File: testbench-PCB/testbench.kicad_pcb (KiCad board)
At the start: 2 copper layers, 41 parts, among them J1 USB_C_Receptacle_USB2.0, J2 AVR-ISP, J3 AVR-JTAG, SW1 SW_Push, U1 ATmega2561-16A, U10 CH340C, U2 Thermistor_module, U3 Rotary_encoder_switch_module, U4 RTC_EEPROM_module, U5 ATmega328P_Xplained_Mini, U7 Matrix_keyboard, U9 USBLC6-2SC6, Y1 X322516MLB4SI

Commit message: Updated footprints, PCB.
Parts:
- added F1: Polyfuse, Fuse:Fuse_1812_4532Metric, F.Cu at (-84.2, 3.73)
- added U6: Relay_module, kit_modules:Relay_module, F.Cu at (164.1, 147.2)
- added U8: LCD_display, kit_modules:LCD_1602A_module, F.Cu at (67.1, 100.3)
- LS1, SW1, U7: moved to B.Cu
- U2: footprint Connector_PinSocket_2.54mm:PinSocket_1x04_P2.54mm_Horizontal -> Connector_PinSocket_2.54mm:PinSocket_1x04_P2.54mm_Vertical; moved to B.Cu
- U3: footprint Connector_PinSocket_2.54mm:PinSocket_1x05_P2.54mm_Horizontal -> kit_modules:Encoder_module
- U4: footprint Connector_PinSocket_2.54mm:PinSocket_1x06_P2.54mm_Horizontal -> Connector_PinSocket_2.54mm:PinSocket_1x06_P2.54mm_Vertical; moved to B.Cu
- moved U5 288.5 mm to (221.0, 101.6)
- moved U4 189.0 mm to (141.0, 115.6), turned to 180 degrees
- moved U2 153.1 mm to (121.9, 115.6), turned to 180 degrees
- moved J1 145.2 mm to (-96.5, -3.89), turned to -90 degrees
- moved U3 141.1 mm to (96.5, 109.2), turned to -90 degrees
- moved R7 133.4 mm to (-60.0, -29.3)
- moved J3 132.9 mm to (-25.3, -25.5), turned to 90 degrees
- moved R6 127.9 mm to (-45.6, -25.5)
- moved R5 123.7 mm to (-60.0, -25.5)
- moved TP2 117.5 mm to (-82.5, -12.8)
- moved FB1 116.1 mm to (-91.4, 5.00)
- moved U7 114.9 mm to (69.8, 111.8), turned to 180 degrees
- moved LS1 114.3 mm to (69.8, 141.0), turned to 180 degrees
- moved C6 113.1 mm to (-31.4, -2.62)
- moved C4 111.9 mm to (-25.3, -5.16), turned to 180 degrees
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
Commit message: Routed osc., USB interface.
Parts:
- added C1: 10u, Capacitor_SMD:C_0805_2012Metric, F.Cu at (36.4, 90.8)
- C2, C3: value 22n -> 22p
- moved TP1 155.5 mm to (35.1, 95.9)
- moved TP2 155.5 mm to (28.8, 95.9)
- moved J1 145.0 mm to (20.0, 82.5)
- moved U10 145.0 mm to (42.8, 83.8)
- moved U9 145.0 mm to (31.4, 82.5)
- moved FB1 144.1 mm to (24.3, 90.9)
- moved F1 143.7 mm to (30.7, 90.2)
- moved JP1 131.8 mm to (42.1, 75.0), turned to 90 degrees
- moved JP2 131.7 mm to (44.7, 75.0), turned to 90 degrees
- moved C5 128.3 mm to (74.6, 94.6)
- moved R8 127.0 mm to (79.0, 93.3), turned to 180 degrees
- moved C2 126.7 mm to (80.3, 96.5), turned to 90 degrees
- moved R4 125.7 mm to (74.6, 92.1), turned to 180 degrees
- moved C6 122.7 mm to (70.8, 65.4)
- moved C3 122.5 mm to (77.8, 96.5), turned to 90 degrees
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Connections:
- net Net-(F1-Pad1) renamed /USB Interface/VBUS
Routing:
- net +5V: track 0.00 -> 23.6 mm
- net Net-(J1-SHIELD): track 0.00 -> 21.1 mm
- net Net-(U10-UD+): track 0.00 -> 17.8 mm
- net Net-(U10-UD-): track 0.00 -> 17.6 mm
- net /USB Interface/VBUS: track 0.00 -> 16.2 mm, vias 0 -> 2
- net Net-(U1-XTAL1): track 0.00 -> 12.0 mm
- net /MCU/RST: track 0.00 -> 10.6 mm
- net Net-(U1-XTAL2): track 0.00 -> 10.5 mm
- net GND: track 0.00 -> 9.67 mm
- net Net-(JP2-A): track 0.00 -> 8.75 mm
- net Net-(J1-CC1): track 0.00 -> 7.16 mm
- net Net-(J1-CC2): track 0.00 -> 6.44 mm
- net Net-(JP1-A): track 0.00 -> 6.29 mm
- net Net-(U1-AREF): track 0.00 -> 4.92 mm
- net Net-(U10-V3): track 0.00 -> 3.88 mm

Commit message: Rearanged PCB, updated footprints.
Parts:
- added D1: LED, LED_SMD:LED_0805_2012Metric, F.Cu at (175.4, 154.4)
- added D2: LED, LED_SMD:LED_0805_2012Metric, F.Cu at (168.6, 154.2)
- added R15: 500R, Resistor_SMD:R_0805_2012Metric, F.Cu at (172.2, 148.0)
- added R16: 500R, Resistor_SMD:R_0805_2012Metric, F.Cu at (167.8, 148.0)
- LS1, SW1, U2, U4, U7: moved to F.Cu
- U5: value ATmega328P_Xplained_Mini -> ATmega328P_Xplained_mini; footprint kit_modules:ATmega328P_Xplained_Mini -> kit_modules:ATmega328P_Xplained_mini
- moved R11 172.5 mm to (211.4, 72.5)
- moved R10 172.5 mm to (211.4, 69.6)
- moved R12 172.5 mm to (211.4, 75.5)
- moved R9 172.5 mm to (211.4, 66.6)
- moved SW1 162.2 mm to (159.7, 152.4), turned to 0 degrees
- moved R3 153.7 mm to (157.8, 146.7), turned to 0 degrees
- moved J2 147.5 mm to (143.0, 153.1), turned to 90 degrees
- moved R5 145.4 mm to (138.1, 151.1)
- moved R6 145.4 mm to (152.4, 151.1)
- moved R7 145.4 mm to (138.1, 147.3)
- moved R13 143.6 mm to (133.0, 42.2), turned to -90 degrees
- moved R14 127.6 mm to (60.3, 43.7)
- moved U6 124.5 mm to (142.5, 38.7), turned to 180 degrees
- moved J3 115.9 mm to (118.5, 151.8)
- moved LS1 115.8 mm to (59.9, 36.1), turned to 0 degrees
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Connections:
- U1 pad 30: unconnected-(U1-PD5-Pad30) -> /ATmega328P module/DUT_D4
- U1 pad 31: unconnected-(U1-PD6-Pad31) -> /ATmega328P module/DUT_D3
- U1 pad 32: unconnected-(U1-PD7-Pad32) -> /ATmega328P module/DUT_D2
- U1 pad 33: unconnected-(U1-PG0-Pad33) -> /ATmega328P module/DUT_D1
- U1 pad 34: unconnected-(U1-PG1-Pad34) -> /ATmega328P module/DUT_D0
- U1 pad 4: unconnected-(U1-PE2-Pad4) -> /MCU/LED1
- U1 pad 5: unconnected-(U1-PE3-Pad5) -> /MCU/LED2
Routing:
- net Net-(JP1-A): track 6.29 -> 14.2 mm
- net +5V: track 23.6 -> 19.2 mm
- net Net-(J1-SHIELD): track 21.1 -> 17.0 mm
- net Net-(JP2-A): track 8.75 -> 12.2 mm
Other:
- board outline added: 171.4 x 125.1 mm
- board text added: "Matrix keyboard"
- board text added: "Speaker"
- board text added: "USB C"

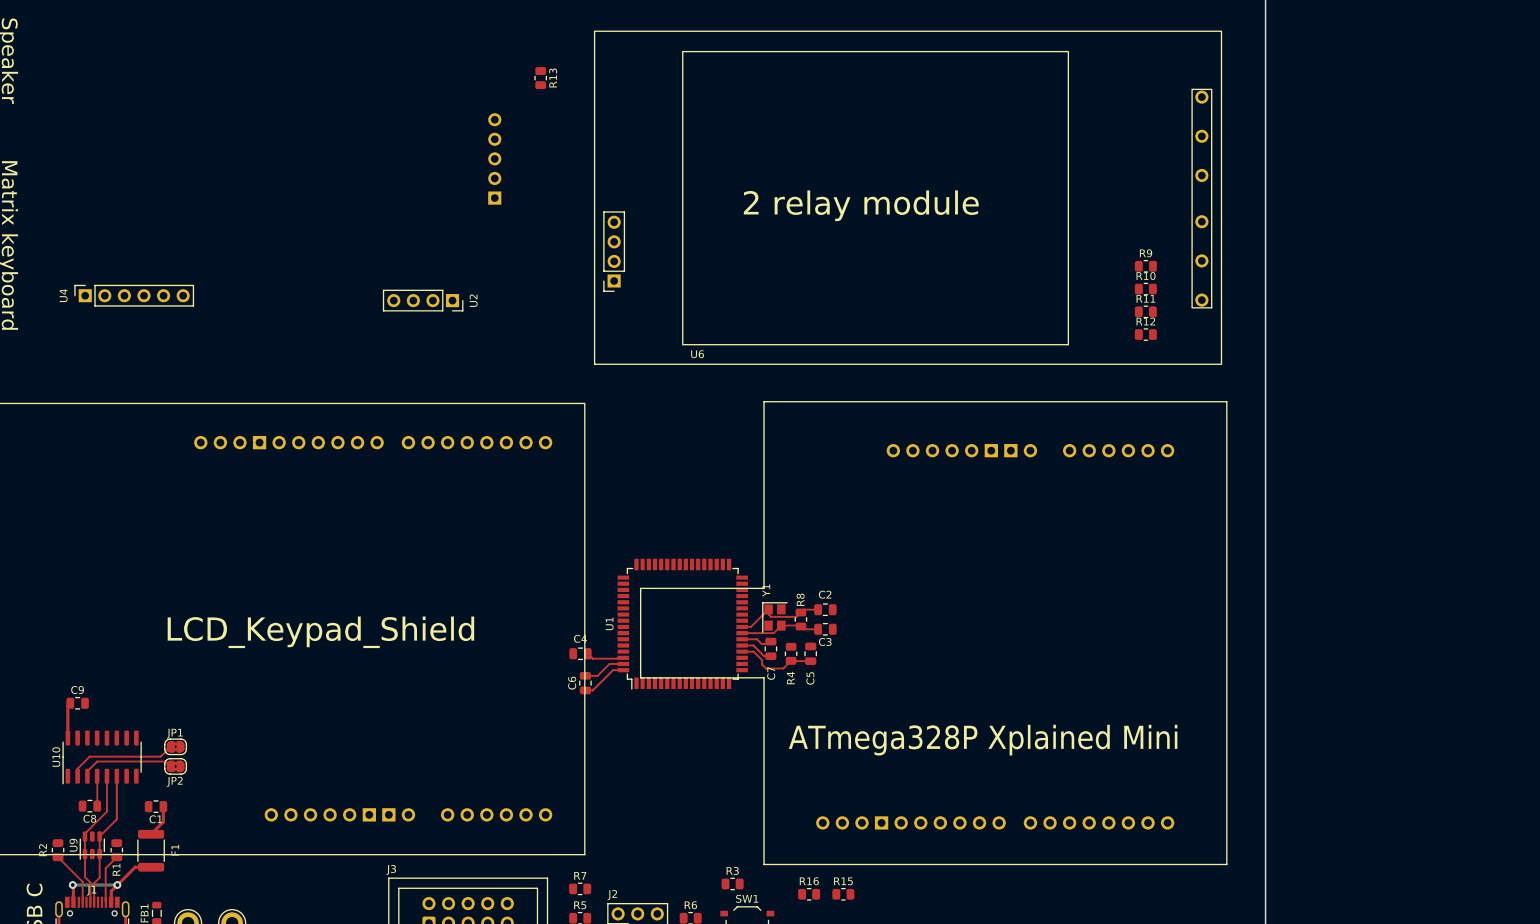
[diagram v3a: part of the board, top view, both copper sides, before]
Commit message: Fixed footprints in schematics.
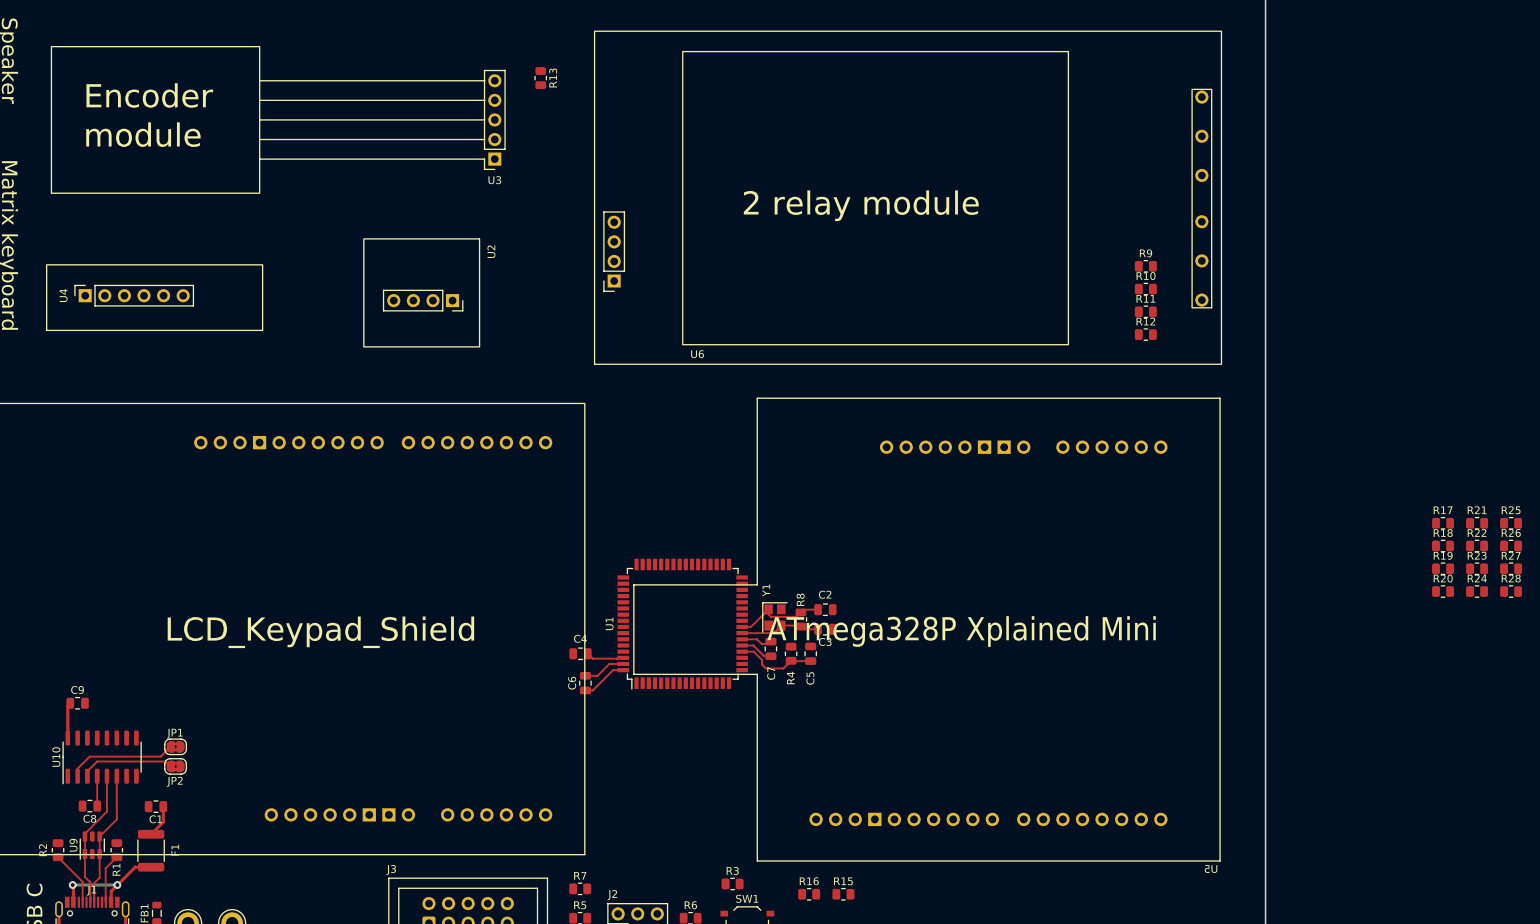
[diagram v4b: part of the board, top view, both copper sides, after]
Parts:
- added R17: 1k, Resistor_SMD:R_0805_2012Metric, F.Cu at (249.9, 99.9)
- added R18: 1k, Resistor_SMD:R_0805_2012Metric, F.Cu at (249.9, 102.9)
- added R19: 1k, Resistor_SMD:R_0805_2012Metric, F.Cu at (249.9, 105.8)
- added R20: 1k, Resistor_SMD:R_0805_2012Metric, F.Cu at (249.9, 108.8)
- added R21: 1k, Resistor_SMD:R_0805_2012Metric, F.Cu at (254.4, 99.9)
- added R22: 1k, Resistor_SMD:R_0805_2012Metric, F.Cu at (254.4, 102.9)
- added R23: 1k, Resistor_SMD:R_0805_2012Metric, F.Cu at (254.4, 105.8)
- added R24: 1k, Resistor_SMD:R_0805_2012Metric, F.Cu at (254.4, 108.8)
- added R25: 1k, Resistor_SMD:R_0805_2012Metric, F.Cu at (258.8, 99.9)
- added R26: 1k, Resistor_SMD:R_0805_2012Metric, F.Cu at (258.8, 102.9)
- added R27: 1k, Resistor_SMD:R_0805_2012Metric, F.Cu at (258.8, 105.8)
- added R28: 1k, Resistor_SMD:R_0805_2012Metric, F.Cu at (258.8, 108.8)
- U2: footprint Connector_PinSocket_2.54mm:PinSocket_1x04_P2.54mm_Vertical -> kit_modules:Thermistor_module
- U3: footprint kit_modules:Encoder_module -> kit_modules:Rotary_encoder_module
- U4: footprint Connector_PinSocket_2.54mm:PinSocket_1x06_P2.54mm_Vertical -> kit_modules:RTC_module
- U5: value ATmega328P_Xplained_mini -> ~
- moved U5 0.99 mm to (221.1, 144.8)
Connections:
- U5 pad 21: unconnected-(U5-~{RESET}/PC6-Pad21) -> /ATmega328P module/DUT_D0
- U5 pad 27: unconnected-(U5-PC0-Pad27) -> /ATmega328P module/DUT_D1
- U5 pad 28: unconnected-(U5-PC1-Pad28) -> /ATmega328P module/DUT_D2
- U5 pad 29: unconnected-(U5-PC2-Pad29) -> /ATmega328P module/DUT_D3
- U5 pad 30: unconnected-(U5-PC3-Pad30) -> /ATmega328P module/DUT_D4
- U5 pad 31: unconnected-(U5-PC4-Pad31) -> /ATmega328P module/DUT_D5
- U5 pad 32: unconnected-(U5-PC5-Pad32) -> /ATmega328P module/DUT_D6

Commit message: Routing the PCB.
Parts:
- added C7: 100n, Capacitor_SMD:C_0805_2012Metric, F.Cu at (109.2, 108.9)
- added REF**: MountingHole_3.2mm_M3_ISO7380_Pad, MountingHole:MountingHole_3.2mm_M3_ISO7380_Pad, F.Cu at (127.0, 31.8)
- added REF**: MountingHole_3.2mm_M3_ISO7380_Pad, MountingHole:MountingHole_3.2mm_M3_ISO7380_Pad, F.Cu at (43.2, 34.9)
- added REF**: MountingHole_3.2mm_M3_ISO7380_Pad, MountingHole:MountingHole_3.2mm_M3_ISO7380_Pad, F.Cu at (219.7, 31.1)
- added REF**: MountingHole_3.2mm_M3_ISO7380_Pad, MountingHole:MountingHole_3.2mm_M3_ISO7380_Pad, F.Cu at (219.7, 157.5)
- added REF**: MountingHole_3.2mm_M3_ISO7380_Pad, MountingHole:MountingHole_3.2mm_M3_ISO7380_Pad, F.Cu at (42.5, 153.7)
- added REF**: MountingHole_3.2mm_M3_ISO7380_Pad, MountingHole:MountingHole_3.2mm_M3_ISO7380_Pad, F.Cu at (134.0, 158.1)
- moved D1 73.3 mm to (102.2, 159.4)
- moved R3 72.9 mm to (85.1, 151.7)
- moved SW1 72.9 mm to (87.0, 157.4)
- moved D2 72.9 mm to (95.9, 159.2)
- moved R16 71.6 mm to (96.5, 154.9)
- moved R15 70.3 mm to (102.2, 154.8)
- moved R18 57.3 mm to (196.8, 81.3), turned to 90 degrees
- moved U7 56.0 mm to (43.2, 108.0)
- moved R19 55.1 mm to (200.7, 81.3), turned to -90 degrees
- moved R20 54.8 mm to (202.6, 81.3), turned to 90 degrees
- moved R17 54.5 mm to (198.8, 81.3), turned to -90 degrees
- moved R22 54.4 mm to (204.5, 81.3), turned to 90 degrees
- moved R14 53.0 mm to (43.5, 94.0)
- moved LS1 53.0 mm to (43.2, 86.4)
- moved R23 52.2 mm to (208.3, 81.3), turned to -90 degrees
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- renumbered C7 to C11
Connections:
- D1 pad 1: /MCU/LED1 -> Net-(D1-K)
- D1 pad 2: Net-(D1-A) -> +5V
- D2 pad 1: /MCU/LED2 -> Net-(D2-K)
- D2 pad 2: Net-(D2-A) -> /MCU/LED2
- J3 pad 1: /MCU/TCK -> /Kit modules/K2-NC
- J3 pad 3: /MCU/TDO -> /Kit modules/K1-NO
- J3 pad 5: /MCU/TMS -> /Kit modules/K1-NC
- J3 pad 9: /MCU/TDI -> /Kit modules/K2-NO
- R13 pad 2: /Kit modules/SW -> /Kit modules/ENC.SW
- R15 pad 1: Net-(D1-A) -> Net-(D1-K)
- R16 pad 1: Net-(D2-A) -> Net-(D2-K)
- R5 pad 1: /MCU/SCK -> /ATmega328P module/DUT_D20
- U1 pad 10: unconnected-(U1-PB0-Pad10) -> /ATmega328P module/DUT_D17
- U1 pad 11: /MCU/SCK -> /ATmega328P module/DUT_D20
- U1 pad 12: /MCU/MOSI -> /ATmega328P module/DUT_D19
- U1 pad 13: /MCU/MISO -> /ATmega328P module/DUT_D18
- U1 pad 14: unconnected-(U1-PB4-Pad14) -> /ATmega328P module/DUT_D16
- U1 pad 15: unconnected-(U1-PB5-Pad15) -> /ATmega328P module/DUT_D15
- U1 pad 16: unconnected-(U1-PB6-Pad16) -> /ATmega328P module/DUT_D14
- U1 pad 17: unconnected-(U1-PB7-Pad17) -> /ATmega328P module/DUT_D13
- U1 pad 18: unconnected-(U1-PG3-Pad18) -> /ATmega328P module/DUT_D12
- U1 pad 19: unconnected-(U1-PG4-Pad19) -> /ATmega328P module/DUT_D11
- U1 pad 27: /MCU/RXD1 -> /ATmega328P module/DUT_D8
- U1 pad 28: /MCU/TXD1 -> /ATmega328P module/DUT_D7
- U1 pad 29: unconnected-(U1-PD4-Pad29) -> /ATmega328P module/DUT_D9
- U1 pad 30: /ATmega328P module/DUT_D4 -> /ATmega328P module/DUT_D10
- U1 pad 31: /ATmega328P module/DUT_D3 -> /ATmega328P module/DUT_D6
- U1 pad 32: /ATmega328P module/DUT_D2 -> /ATmega328P module/DUT_D5
- U1 pad 33: /ATmega328P module/DUT_D1 -> /ATmega328P module/DUT_D4
- U1 pad 34: /ATmega328P module/DUT_D0 -> /ATmega328P module/DUT_D3
- U1 pad 35: unconnected-(U1-PC0-Pad35) -> /ATmega328P module/DUT_D2
- U1 pad 36: unconnected-(U1-PC1-Pad36) -> /ATmega328P module/DUT_D1
- U1 pad 37: unconnected-(U1-PC2-Pad37) -> /ATmega328P module/DUT_D0
- U1 pad 38: unconnected-(U1-PC3-Pad38) -> /Kit modules/LCD_D0
- U1 pad 39: unconnected-(U1-PC4-Pad39) -> /Kit modules/LCD_D1
- U1 pad 4: /MCU/LED1 -> /Kit modules/Speaker_IN
- U1 pad 40: unconnected-(U1-PC5-Pad40) -> /Kit modules/LCD_D2
- U1 pad 41: unconnected-(U1-PC6-Pad41) -> /Kit modules/LCD_D3
- U1 pad 42: unconnected-(U1-PC7-Pad42) -> /Kit modules/LCD_D4
- U1 pad 43: /Kit modules/Speaker_IN -> /Kit modules/LCD_D5
- U1 pad 44: unconnected-(U1-PA7-Pad44) -> /Kit modules/KEY_D0
- U1 pad 45: unconnected-(U1-PA6-Pad45) -> /Kit modules/KEY_D1
- U1 pad 46: unconnected-(U1-PA5-Pad46) -> /Kit modules/KEY_D2
- U1 pad 47: unconnected-(U1-PA4-Pad47) -> /Kit modules/KEY_D3
- U1 pad 48: unconnected-(U1-PA3-Pad48) -> /Kit modules/KEY_D4
- U1 pad 49: unconnected-(U1-PA2-Pad49) -> /Kit modules/KEY_D5
- U1 pad 5: /MCU/LED2 -> unconnected-(U1-PE3-Pad5)
- U1 pad 50: unconnected-(U1-PA1-Pad50) -> /Kit modules/KEY_D6
- U1 pad 51: unconnected-(U1-PA0-Pad51) -> /Kit modules/KEY_D7
- U1 pad 54: /MCU/TDI -> /Kit modules/K2-NO
- U1 pad 55: /MCU/TDO -> /Kit modules/K1-NO
- U1 pad 56: /MCU/TMS -> /Kit modules/K1-NC
- U1 pad 57: /MCU/TCK -> /Kit modules/K2-NC
- U1 pad 58: unconnected-(U1-PF3-Pad58) -> /Kit modules/K1-IN
- U1 pad 59: unconnected-(U1-PF2-Pad59) -> /Kit modules/K2-IN
- U1 pad 7: unconnected-(U1-PE5-Pad7) -> /Kit modules/ENC.A
- U1 pad 8: unconnected-(U1-PE6-Pad8) -> /Kit modules/ENC.B
- U1 pad 9: unconnected-(U1-PE7-Pad9) -> /Kit modules/ENC.SW
- U3 pad 1: /Kit modules/A -> /Kit modules/ENC.A
- U3 pad 2: /Kit modules/B -> /Kit modules/ENC.B
- U3 pad 3: /Kit modules/SW -> /Kit modules/ENC.SW
- U5 pad 1: unconnected-(U5-PD0-Pad1) -> /ATmega328P module/DUT_D7
- U5 pad 10: unconnected-(U5-PB1-Pad10) -> /ATmega328P module/DUT_D16
- U5 pad 11: unconnected-(U5-PB2-Pad11) -> /ATmega328P module/DUT_D17
- U5 pad 12: /ATmega328P module/MOSI -> /ATmega328P module/DUT_D18
- U5 pad 13: /ATmega328P module/MISO -> /ATmega328P module/DUT_D19
- U5 pad 14: /ATmega328P module/SCK -> /ATmega328P module/DUT_D20
- U5 pad 2: unconnected-(U5-PD1-Pad2) -> /ATmega328P module/DUT_D8
- U5 pad 3: unconnected-(U5-PD2-Pad3) -> /ATmega328P module/DUT_D9
- U5 pad 4: unconnected-(U5-PD3-Pad4) -> /ATmega328P module/DUT_D10
- U5 pad 5: unconnected-(U5-PD4-Pad5) -> /ATmega328P module/DUT_D11
- U5 pad 6: unconnected-(U5-PD5-Pad6) -> /ATmega328P module/DUT_D12
- U5 pad 7: unconnected-(U5-PD6-Pad7) -> /ATmega328P module/DUT_D13
- U5 pad 8: unconnected-(U5-PD7-Pad8) -> /ATmega328P module/DUT_D14
- U5 pad 9: unconnected-(U5-PB0-Pad9) -> /ATmega328P module/DUT_D15
- U7 pad 1: unconnected-(U7-ROW1-Pad1) -> /Kit modules/KEY_D0
- U7 pad 2: unconnected-(U7-ROW2-Pad2) -> /Kit modules/KEY_D1
- U7 pad 3: unconnected-(U7-ROW3-Pad3) -> /Kit modules/KEY_D2
- U7 pad 4: unconnected-(U7-ROW4-Pad4) -> /Kit modules/KEY_D3
- U7 pad 5: unconnected-(U7-COL1-Pad5) -> /Kit modules/KEY_D4
- U7 pad 6: unconnected-(U7-COL2-Pad6) -> /Kit modules/KEY_D5
- U7 pad 7: unconnected-(U7-COL3-Pad7) -> /Kit modules/KEY_D6
- U7 pad 8: unconnected-(U7-COL4-Pad8) -> /Kit modules/KEY_D7
- U8 pad 1: unconnected-(U8-D4-Pad1) -> (no net)
- U8 pad 10: /Kit modules/LCD_AO -> /Kit modules/LCD_D5
- U8 pad 17: (no net) -> /Kit modules/LCD_D6
- U8 pad 19: (no net) -> +5V
- U8 pad 2: unconnected-(U8-D5-Pad2) -> (no net)
- U8 pad 20: (no net) -> GND
- U8 pad 21: (no net) -> GND
- U8 pad 23: (no net) -> /Kit modules/LCD_AO
- U8 pad 3: unconnected-(U8-D6-Pad3) -> (no net)
- U8 pad 4: unconnected-(U8-D7-Pad4) -> (no net)
- U8 pad 5: unconnected-(U8-RS-Pad5) -> /Kit modules/LCD_D0
- U8 pad 6: unconnected-(U8-E-Pad6) -> /Kit modules/LCD_D1
- U8 pad 7: unconnected-(U8-RST-Pad7) -> /Kit modules/LCD_D2
- U8 pad 8: +5V -> /Kit modules/LCD_D3
- U8 pad 9: GND -> /Kit modules/LCD_D4
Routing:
- net /Kit modules/K1-NC: track 0.00 -> 241.3 mm, vias 0 -> 1
- net /Kit modules/K1-NO: track 0.00 -> 226.4 mm, vias 0 -> 1
- net /Kit modules/K2-NC: track 0.00 -> 207.4 mm, vias 0 -> 1
- net /Kit modules/K2-NO: track 0.00 -> 199.0 mm, vias 0 -> 1
- net /Kit modules/I2C_SCL: track 0.00 -> 167.9 mm, vias 0 -> 2
- net /Kit modules/I2C_SDA: track 0.00 -> 161.1 mm, vias 0 -> 2
- net /Kit modules/ENC.B: track 0.00 -> 150.6 mm, vias 0 -> 2
- net /Kit modules/ENC.SW: track 0.00 -> 150.4 mm, vias 0 -> 2
- net /Kit modules/ENC.A: track 0.00 -> 145.4 mm, vias 0 -> 2
- net /Kit modules/Speaker_IN: track 0.00 -> 134.1 mm, vias 0 -> 2
- net /ATmega328P module/DUT_D10: track 0.00 -> 114.6 mm
- net /Kit modules/RTC_SQW: track 0.00 -> 112.4 mm, vias 0 -> 1
- net /ATmega328P module/DUT_D9: track 0.00 -> 110.1 mm
- net /Kit modules/K1-IN: track 0.00 -> 106.9 mm, vias 0 -> 1
- net /Kit modules/K2-IN: track 0.00 -> 106.6 mm, vias 0 -> 1
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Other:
- board size 171.4 x 125.1 mm -> 185.4 x 134.6 mm
